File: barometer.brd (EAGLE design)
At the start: 58.4 x 40.4 mm, 105 parts, among them IC1 TPS5410, IC2 ZPA2326-0311A-R, IC3 MIC5225-3.3v, Q1 BC817, U1 LTC2850, U2 PCA9306, U3 DAC8574, U4 XTR117, U5 XC6215XC6215B182NR, U6 MAX3221, U7 Tiny85-20-SMT, X1 1751248, X2 1751264

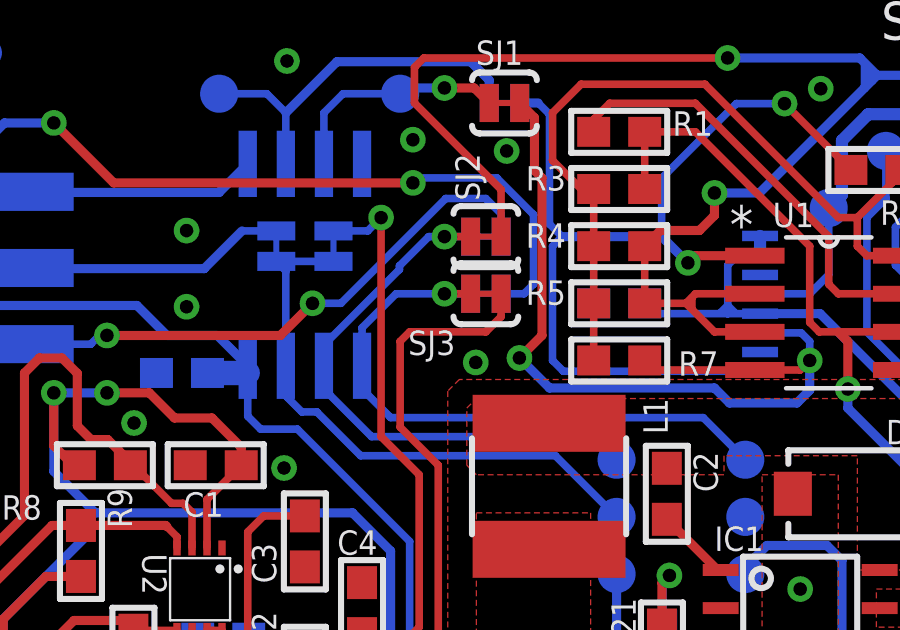
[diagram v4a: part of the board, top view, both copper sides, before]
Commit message: Remove trace in solder jumper SJ3
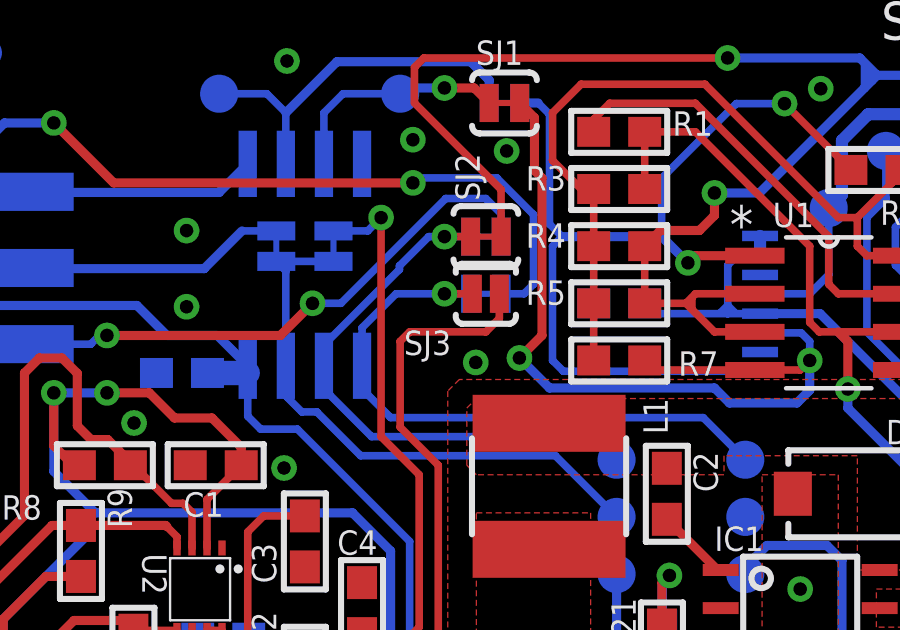
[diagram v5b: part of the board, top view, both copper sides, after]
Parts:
- SJ3: value SOLDERJUMPERTRACE -> SOLDERJUMPERNO; device SparkFun-Retired-0:SJ_2S-TRACE -> SparkFun-Retired-0:SJ_2S-NO
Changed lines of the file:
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@@
 <attribute name="PROD_ID" value="IC-09092" x="18.0975" y="29.8425" size="1.778" layer="28" rot="MR180" display="off"/>
-</element>
-<element name="SJ3" library="SparkFun-Retired-0" package="SJ_2S-TRACE" value="SOLDERJUMPERTRACE" x="24.13" y="28.89" smashed="yes">
-<attribute name="NAME" x="23.11" y="27.66" size="0.8128" layer="25" font="vector" ratio="18" align="top-right"/>
 </element>
 <element name="SJ9" library="SparkFun-Retired-0" package="SJ_2S-TRACE" value="SOLDERJUMPERTRACE" x="19.05" y="30.4775" smashed="yes" rot="MR90">
@@
 <element name="JP3" library="microbuilder" package="1X03_SMT" value="Analog Output Format 2" x="51" y="18.75" smashed="yes">
 <attribute name="NAME" x="51" y="23.25" size="0.8128" layer="25" font="vector" ratio="18" align="center"/>
+</element>
+<element name="SJ3" library="SparkFun-Retired-0" package="SJ_2S-NO" value="SOLDERJUMPERNO" x="24.13" y="28.89" smashed="yes">
+<attribute name="NAME" x="22.972" y="27.66" size="0.8128" layer="25" font="vector" ratio="18" rot="R180"/>
 </element>
 </elements>
@@
 <signal name="SDA_3V3">
 <contactref element="R11" pad="2"/>
-<contactref element="SJ3" pad="2"/>
-<wire x1="24.638" y1="28.89" x2="24.638" y2="28.128" width="0.254" layer="1"/>
-<wire x1="24.638" y1="28.128" x2="24.13" y2="27.62" width="0.254" layer="1"/>
-<wire x1="24.13" y1="27.62" x2="21.59" y2="27.62" width="0.254" layer="1"/>
+<wire x1="21.59" y1="27.62" x2="24.13" y2="27.62" width="0.254" layer="1"/>
 <wire x1="21.59" y1="27.62" x2="21.2725" y2="27.3025" width="0.254" layer="1"/>
 <wire x1="21.2725" y1="27.3025" x2="21.2725" y2="24.445" width="0.254" layer="1"/>
@@
 <wire x1="10.4" y1="14" x2="9.9" y2="14.5" width="0.3048" layer="1"/>
 <wire x1="12.5" y1="14" x2="10.4" y2="14" width="0.3048" layer="1"/>
+<contactref element="SJ3" pad="2"/>
+<wire x1="24.13" y1="27.62" x2="24.58" y2="28.07" width="0.254" layer="1"/>
+<wire x1="24.58" y1="28.07" x2="24.58" y2="28.89" width="0.254" layer="1"/>
 </signal>
 <signal name="SDA_1V8">
@@
 </signal>
 <signal name="B0">
-<contactref element="SJ3" pad="1"/>
 <contactref element="U7" pad="5"/>
 <contactref element="SJ8" pad="1"/>
@@
 <wire x1="32.7775" y1="23.3575" x2="31.3725" y2="24.7625" width="0.254" layer="16"/>
 <wire x1="21.1375" y1="28.89" x2="22.75" y2="28.89" width="0.254" layer="16"/>
-<wire x1="23.622" y1="28.89" x2="22.75" y2="28.89" width="0.254" layer="1"/>
 <wire x1="23.622" y1="28.89" x2="22.75" y2="28.89" width="0.254" layer="16"/>
+<contactref element="SJ3" pad="1"/>
+<wire x1="23.68" y1="28.89" x2="22.75" y2="28.89" width="0.254" layer="1"/>
 </signal>
 <signal name="B2">
